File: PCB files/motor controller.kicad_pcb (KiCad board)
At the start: 2 copper layers, 84.5 x 62 mm, 33 parts, among them J1 ISP, J2 I2C, J3 Motor Signal, J4 M1, J5 M2, J6 RST_Jump, J7 RST_Jump, SW1 reset, U1 ATmega328-P, Y1 16Mhz

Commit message: added more jumpers
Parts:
- added J10: 5V, Connector_PinHeader_2.54mm:PinHeader_1x01_P2.54mm_Vertical, F.Cu at (119.0, 91.0)
- added J11: 5V, Connector_PinHeader_2.54mm:PinHeader_1x01_P2.54mm_Vertical, F.Cu at (86.0, 62.5)
- added J8: GND, Connector_PinHeader_2.54mm:PinHeader_1x01_P2.54mm_Vertical, F.Cu at (117.5, 80.0)
- added J9: 5V, Connector_PinHeader_2.54mm:PinHeader_1x01_P2.54mm_Vertical, F.Cu at (114.0, 82.5)
- moved C1 2.00 mm to (110.5, 82.9)
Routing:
- net +5V: track 145.1 -> 169.4 mm
- net /DM2: track 72.4 -> 63.7 mm
- net /PM2: track 89.0 -> 81.0 mm
- net /MOSI: track 19.3 -> 23.6 mm
- net GND: track 315.4 -> 319.1 mm
- net /PM1: track 39.1 -> 36.3 mm
- net /M2A: track 23.5 -> 24.9 mm

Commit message: improved design
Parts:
- removed J10, J11, J9: 5V, Connector_PinHeader_2.54mm:PinHeader_1x01_P2.54mm_Vertical
- removed J7: RST_Jump, Connector_PinHeader_2.54mm:PinHeader_1x01_P2.54mm_Vertical
- removed J8: GND, Connector_PinHeader_2.54mm:PinHeader_1x01_P2.54mm_Vertical
- removed R12: Jumper, Resistor_THT:R_Axial_DIN0207_L6.3mm_D2.5mm_P7.62mm_Horizontal
- removed R13: Jumper, Resistor_THT:R_Axial_DIN0207_L6.3mm_D2.5mm_P10.16mm_Horizontal
- C1: footprint Capacitor_THT:CP_Radial_D4.0mm_P2.00mm -> Capacitor_SMD:CP_Elec_6.3x4.5
- C2, C3: footprint Capacitor_THT:C_Disc_D3.4mm_W2.1mm_P2.50mm -> Capacitor_SMD:C_0805_2012Metric
- D1, D2: footprint LED_THT:LED_D3.0mm -> LED_SMD:LED_0805_2012Metric
- J2: value I2C -> SW; footprint Connector_JST:JST_EH_S4B-EH_1x04_P2.50mm_Horizontal -> Button_Switch_THT:SW_DIP_SPSTx05_Slide_9.78x14.88mm_W7.62mm_P2.54mm
- J3: value Motor Signal -> I2C; footprint Connector_PinSocket_2.54mm:PinSocket_1x05_P2.54mm_Vertical -> Connector_JST:JST_EH_S4B-EH_1x04_P2.50mm_Horizontal; moved to F.Cu
- J4: value M1 -> Motor Signal; footprint Connector_JST:JST_EH_S4B-EH_1x04_P2.50mm_Horizontal -> Connector_PinSocket_2.54mm:PinSocket_1x05_P2.54mm_Vertical
- J5: value M2 -> M1
- J6: value RST_Jump -> M2; footprint Connector_PinHeader_2.54mm:PinHeader_1x01_P2.54mm_Vertical -> Connector_JST:JST_EH_S4B-EH_1x04_P2.50mm_Horizontal
- R1: value 10K -> 5K; footprint Resistor_THT:R_Axial_DIN0207_L6.3mm_D2.5mm_P7.62mm_Horizontal -> Resistor_SMD:R_0805_2012Metric
- R10, R11: footprint Resistor_THT:R_Axial_DIN0207_L6.3mm_D2.5mm_P7.62mm_Horizontal -> Resistor_SMD:R_0805_2012Metric
- R2: value 100E -> 5K; footprint Resistor_THT:R_Axial_DIN0207_L6.3mm_D2.5mm_P7.62mm_Horizontal -> Resistor_SMD:R_0805_2012Metric
- R3: value 1K -> 5K; footprint Resistor_THT:R_Axial_DIN0207_L6.3mm_D2.5mm_P7.62mm_Horizontal -> Resistor_SMD:R_0805_2012Metric
- R4: value 470E -> 5K; footprint Resistor_THT:R_Axial_DIN0207_L6.3mm_D2.5mm_P7.62mm_Horizontal -> Resistor_SMD:R_0805_2012Metric
- R5: footprint Resistor_THT:R_Axial_DIN0204_L3.6mm_D1.6mm_P5.08mm_Horizontal -> Resistor_SMD:R_0805_2012Metric
- R6: value 5K -> 10K; footprint Resistor_THT:R_Axial_DIN0204_L3.6mm_D1.6mm_P2.54mm_Vertical -> Resistor_SMD:R_0805_2012Metric
- R7: value 5K -> 100E; footprint Resistor_THT:R_Axial_DIN0204_L3.6mm_D1.6mm_P2.54mm_Vertical -> Resistor_SMD:R_0805_2012Metric
- R8: value 5K -> 1K; footprint Resistor_THT:R_Axial_DIN0204_L3.6mm_D1.6mm_P2.54mm_Vertical -> Resistor_SMD:R_0805_2012Metric
- R9: value 5K -> 470E; footprint Resistor_THT:R_Axial_DIN0204_L3.6mm_D1.6mm_P2.54mm_Vertical -> Resistor_SMD:R_0805_2012Metric
- Y1: footprint Crystal:Crystal_HC49-4H_Vertical -> Crystal:Crystal_SMD_HC49-SD
- moved J4 66.0 mm to (131.5, 77.5)
- moved J3 47.0 mm to (88.8, 57.5), turned to 0 degrees
- moved R10 46.6 mm to (81.0, 67.6)
- moved R7 46.0 mm to (80.0, 105.5), turned to 90 degrees
- moved R3 39.9 mm to (115.0, 88.5), turned to -90 degrees
- moved R11 38.6 mm to (84.0, 67.6)
- moved R8 38.6 mm to (74.0, 67.5), turned to 90 degrees
- moved R2 36.2 mm to (112.5, 88.5), turned to -90 degrees
- moved R9 33.9 mm to (75.0, 95.0), turned to 180 degrees
- moved R5 33.6 mm to (120.0, 88.5), turned to -90 degrees
- moved D2 31.3 mm to (82.5, 95.0), turned to 0 degrees
- moved C1 28.3 mm to (95.0, 106.5), turned to 180 degrees
- moved R1 27.3 mm to (110.0, 88.5), turned to -90 degrees
- moved J2 25.7 mm to (109.9, 82.6), turned to 90 degrees
- moved R4 17.9 mm to (117.5, 88.5), turned to -90 degrees
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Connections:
- BZ1 pad 1: Net-(BZ1-Pad1) -> Net-(BZ1--)
- D1 pad 1: Net-(D1-Pad1) -> Net-(D1-K)
- D2 pad 1: Net-(D2-Pad1) -> Net-(D2-K)
- J1 pad 5: /RST2 -> /RST
- J2 pad 1: +5V -> /S1
- J2 pad 2: /SCL -> /S2
- J2 pad 3: /SDA -> /S3
- J2 pad 4: GND -> /S4
- J3 pad 1: /DM1 -> +5V
- J3 pad 2: /PM1 -> /SCL
- J3 pad 3: /DM2 -> /SDA
- J3 pad 4: /PM2 -> GND
- J4 pad 1: +5V -> /DM1
- J4 pad 2: GND -> /PM1
- J4 pad 3: /M1A -> /DM2
- J4 pad 4: /M1B -> /PM2
- J5 pad 3: /M2A -> /M1A
- J5 pad 4: /M2B -> /M1B
- J6 pad 1: /RST1 -> +5V
- R1 pad 2: /RST1 -> /S1
- R2 pad 1: Net-(BZ1-Pad1) -> +5V
- R2 pad 2: /BUZZ -> /S2
- R3 pad 1: Net-(D1-Pad1) -> +5V
- R3 pad 2: GND -> /S3
- R4 pad 1: Net-(D2-Pad1) -> +5V
- R4 pad 2: GND -> /S4
- R5 pad 1: /S1 -> +5V
- R5 pad 2: GND -> /S5
- R6 pad 1: /S2 -> +5V
- R6 pad 2: GND -> /RST1
- R7 pad 1: /S3 -> Net-(BZ1--)
- R7 pad 2: GND -> /BUZZ
- R8 pad 1: /S4 -> Net-(D1-K)
- R9 pad 1: /S5 -> Net-(D2-K)
- U1 pad 1: /RST1 -> /RST
- U1 pad 11: /BUZZ -> /LED
- U1 pad 12: /PM2 -> /BUZZ
- U1 pad 13: /S1 -> /S2
- U1 pad 14: /DM2 -> /S1
- U1 pad 15: /LED -> /PM2
- U1 pad 2: /S5 -> /DM1
- U1 pad 23: /DM1 -> /S5
- U1 pad 24: /S2 -> /S4
- U1 pad 26: /S4 -> /DM2
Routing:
- net +5V: track 169.4 -> 279.4 mm, vias 0 -> 2
- net GND: track 319.1 -> 401.6 mm
- net /RST: track 0.00 -> 75.2 mm, vias 0 -> 1
- net /S5: track 3.22 -> 52.1 mm, vias 0 -> 1
- net /S4: track 6.17 -> 50.3 mm, vias 0 -> 1
- net /S3: track 6.23 -> 48.6 mm, vias 0 -> 1
- net /S2: track 6.25 -> 47.7 mm, vias 0 -> 1
- net /DM1: track 25.7 -> 59.5 mm, vias 0 -> 1
- net /PM2: track 81.0 -> 49.9 mm
- net /M2A: track 24.9 -> 52.5 mm
- net /DM2: track 63.7 -> 41.0 mm
- net /S1: track 14.6 -> 36.7 mm, vias 0 -> 1
- net /SCK: track 7.43 -> 25.0 mm
- net /M2B: track 20.2 -> 35.7 mm
- net /RST1: track 27.1 -> 12.2 mm
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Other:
- board text added: "I2C"
- board text added: "ISP"
- board text added: "MOTOR 1"
- board text added: "MOTOR 2"
- board text added: "MOTOR CONTROLLER H.A.T"

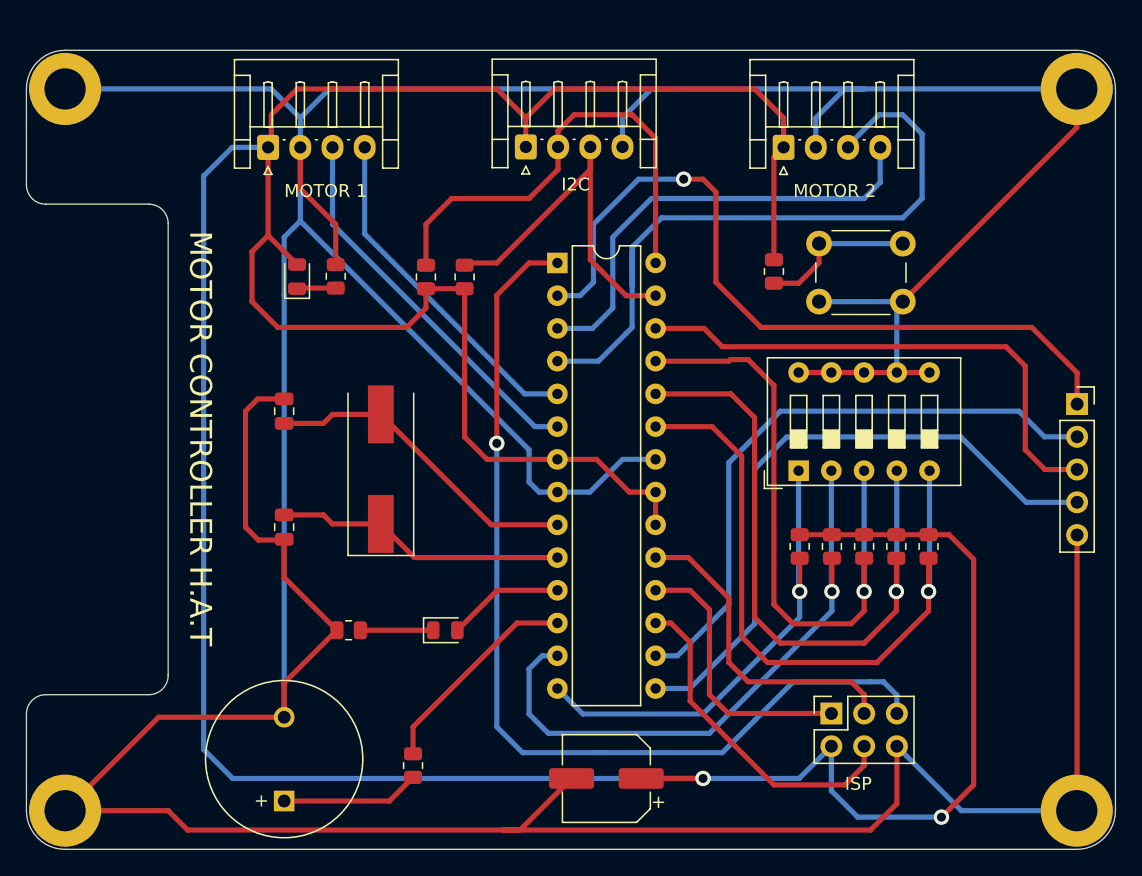
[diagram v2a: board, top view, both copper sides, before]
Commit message: increassded power track width
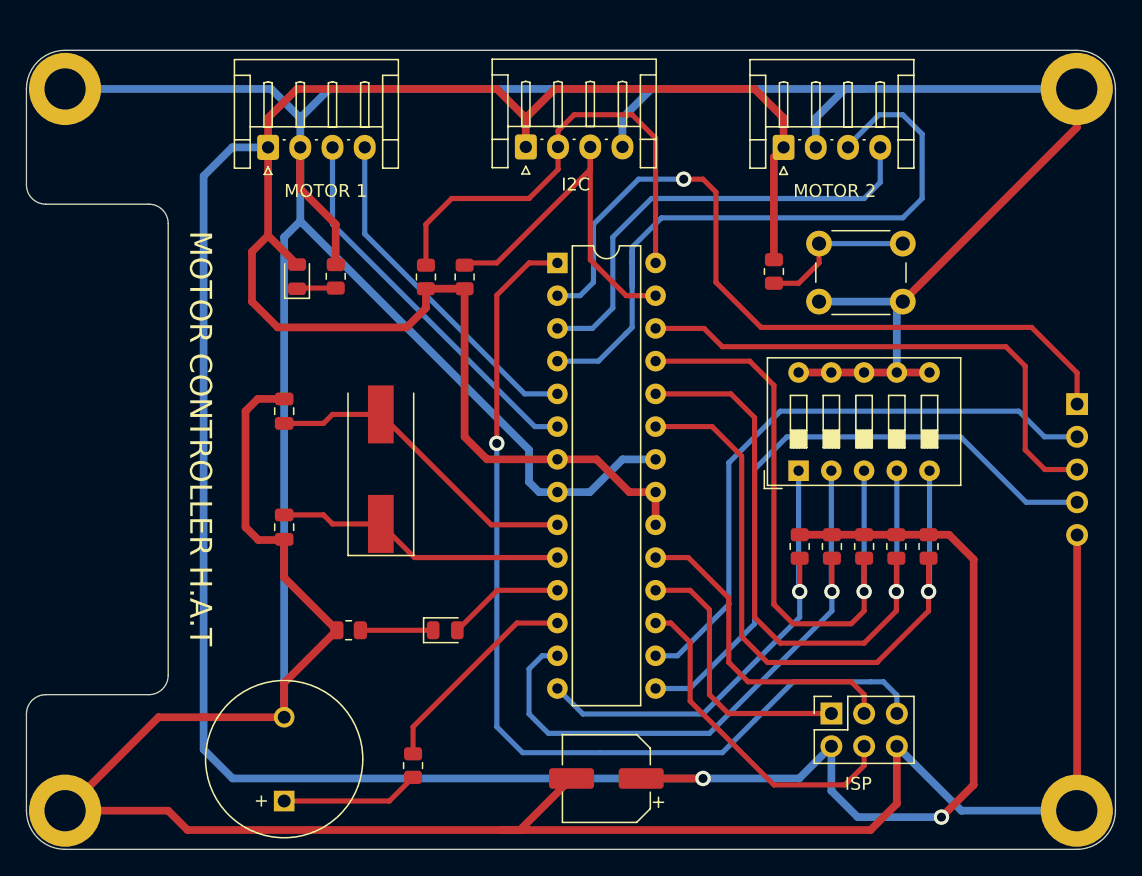
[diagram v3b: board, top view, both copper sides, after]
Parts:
- J4: moved to B.Cu
- turned J4 to 180 degrees

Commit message: updated track width
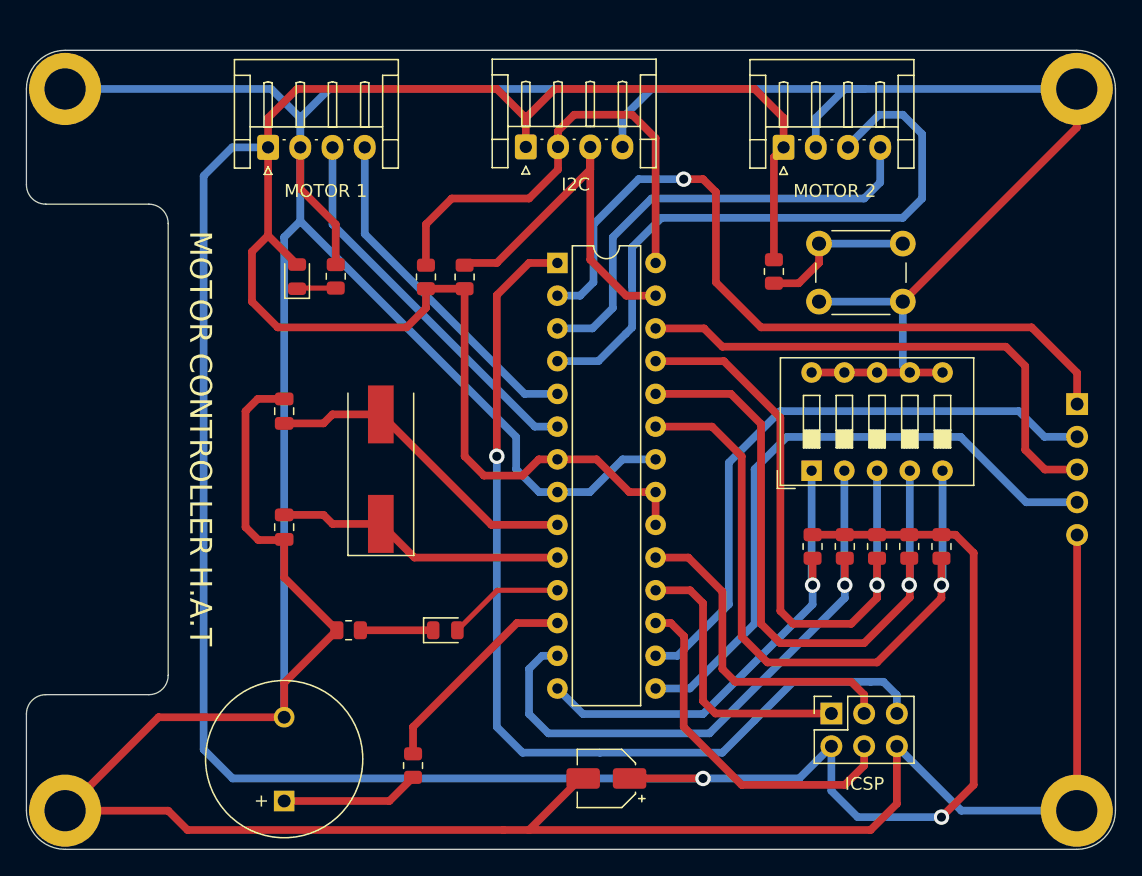
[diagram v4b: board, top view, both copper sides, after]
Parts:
- C1: footprint Capacitor_SMD:CP_Elec_6.3x4.5 -> Capacitor_SMD:CP_Elec_4x3.9
- moved J2 1.01 mm to (110.9, 82.6)
- moved R1 1.00 mm to (111.0, 88.5)
- moved R2 1.00 mm to (113.5, 88.5)
- moved R3 1.00 mm to (116.0, 88.5)
- moved R4 1.00 mm to (118.5, 88.5)
- moved R5 1.00 mm to (121.0, 88.5)
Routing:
- net +5V: track 279.4 -> 281.5 mm
- net /MOSI: track 26.2 -> 27.7 mm
- net /S3: track 48.5 -> 47.2 mm
- net GND: track 401.6 -> 400.6 mm
- net /SCK: track 25.0 -> 25.6 mm
- net /MISO: track 21.5 -> 22.1 mm
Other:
- board text added: "ICSP"
- board text removed: "ISP"
